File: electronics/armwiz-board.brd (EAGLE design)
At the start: 98.8 x 51 mm, 89 parts, among them IC1 MCP3424, J1 SD_MICRO_SDIO_1BIT, J2 CORTEX_DEBUGSMD, U1 STM32F10XRXT6, U4 MIC5219-3.3V, X2 M12_BOTTOM_CONTACTS_FPC_1MM, Y1 32.768kHz, Y3 32.768kHz

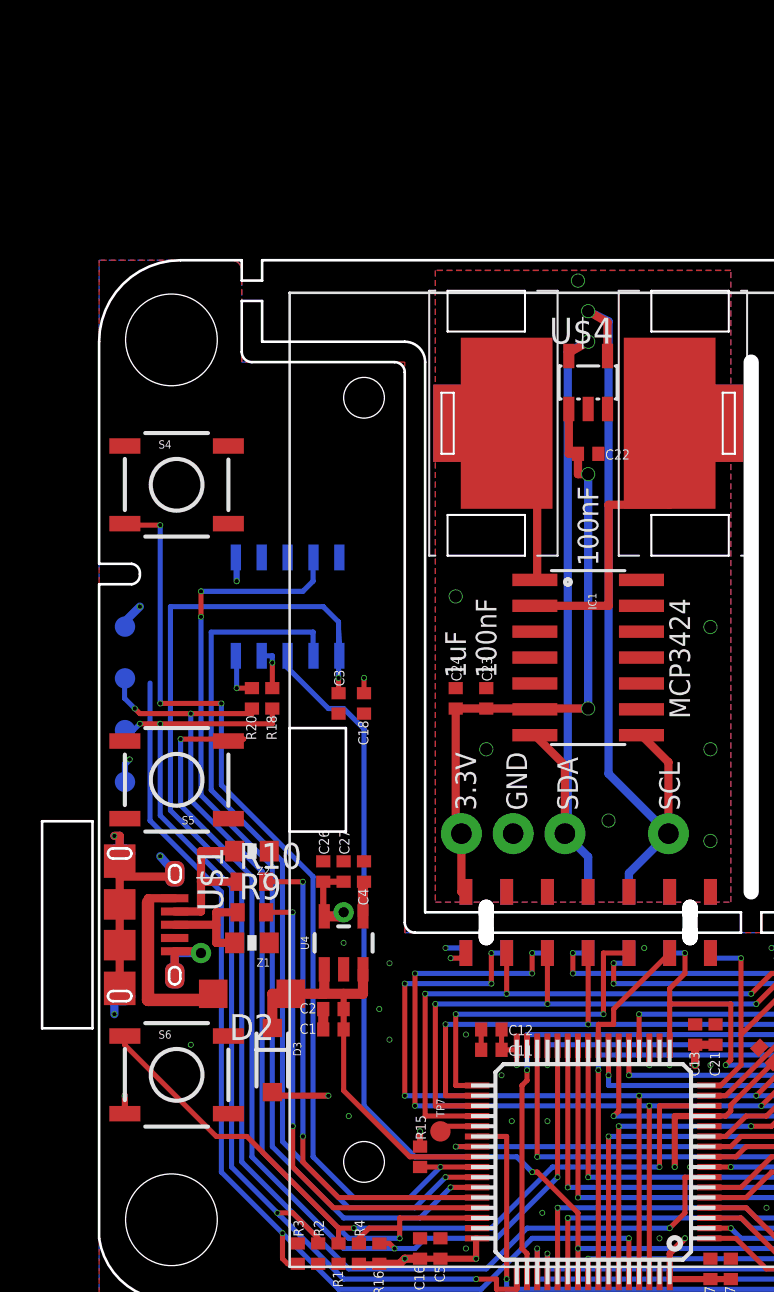
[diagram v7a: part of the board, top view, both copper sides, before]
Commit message: Added ESP8266 module footprint.
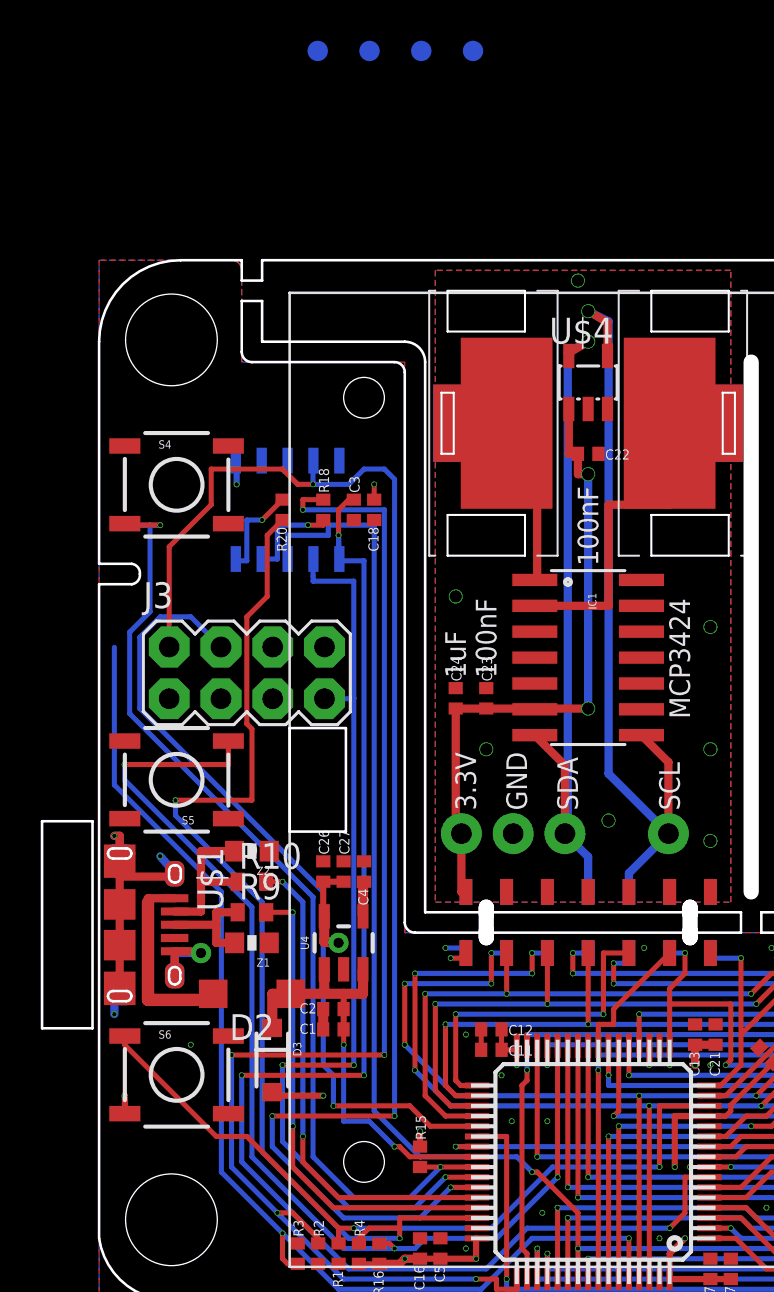
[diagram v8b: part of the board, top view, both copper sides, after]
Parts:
- removed TP7: (no value), PaxInstruments-Connectors:PAD_1MM
- added J3: (no value), SparkFun-Connectors:2X4
- moved TP9 39.7 mm to (18.4, 61.3), turned to 270 degrees
- moved TP6 36.4 mm to (15.8, 61.3), turned to 270 degrees
- moved TP5 33.0 mm to (13.3, 61.3), turned to 270 degrees
- moved TP8 29.8 mm to (10.7, 61.3), turned to 270 degrees
- moved R18 9.58 mm to (11.0, 38.8), turned to 270 degrees
- moved C3 9.53 mm to (12.5, 38.8)
- moved C18 9.51 mm to (13.5, 38.8)
- moved R20 9.37 mm to (9.00, 38.8)
- moved J2 4.75 mm to (9.25, 38.8)
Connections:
- net N$5 renamed SWDCLK_M
- removed net N$13: J2.2, R20.2
- removed net PC6: TP7.P$1, U1.37
- new net SWCLK_M: TP6.P$1
- new net SWDIO_M: J2.2, R20.2, TP5.P$1
- new net WIFI_EN: J3.4, U1.37
- net 3.3V: now also J3.8
- net GND: now also J3.1
- net SWCLK: no longer TP6.P$1
- net SWDIO: no longer TP5.P$1
- net USART1_RX: now also J3.2
- net USART1_TX: now also J3.7
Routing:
- net WIFI_EN: track 0.00 -> 39.4 mm, vias 0 -> 1
- net USART1_RX: track 47.7 -> 71.5 mm, vias 3 -> 4
- net SWCLK: track 51.6 -> 65.5 mm, vias 4 -> 5
- net LCD_SCK_(SPI3_SCK_SWO): track 75.8 -> 85.7 mm
- net SWDIO: track 46.6 -> 53.1 mm, vias 3 -> 2
- net SWDIO_M: track 0.00 -> 4.82 mm, vias 0 -> 1
- net USART1_TX: track 44.1 -> 47.1 mm, vias 1 -> 3
- net SWDCLK_M: track 2.11 -> 4.93 mm
- net BOOT0: track 52.9 -> 55.4 mm
- net N$13: track 2.38 -> 0.00 mm, vias 1 -> 0
- net SW_E_(BOOT1): track 51.4 -> 53.7 mm
- net PC6: track 1.90 -> 0.00 mm
- net NRST: track 71.3 -> 69.5 mm, vias 2 -> 4
- net CAN_RX: track 98.8 -> 97.3 mm
- net GND: track 26.8 -> 25.6 mm, vias 83 -> 77
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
